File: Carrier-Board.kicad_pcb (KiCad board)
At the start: 4 copper layers, 92 x 96 mm, 50 parts, among them J1 CONN_3-6318491-6, J10 Conn_02x03_Odd_Even, J2 Conn_01x0, J3 Conn_02x26_Odd_Even, J4 SI-51009-F, J5 Conn_02x26_Odd_Even, J6 Conn_01x03_Male, J7 Conn_01x03_Male, J8 Conn_01x06_Male, J9 Conn_02x04_Odd_Even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

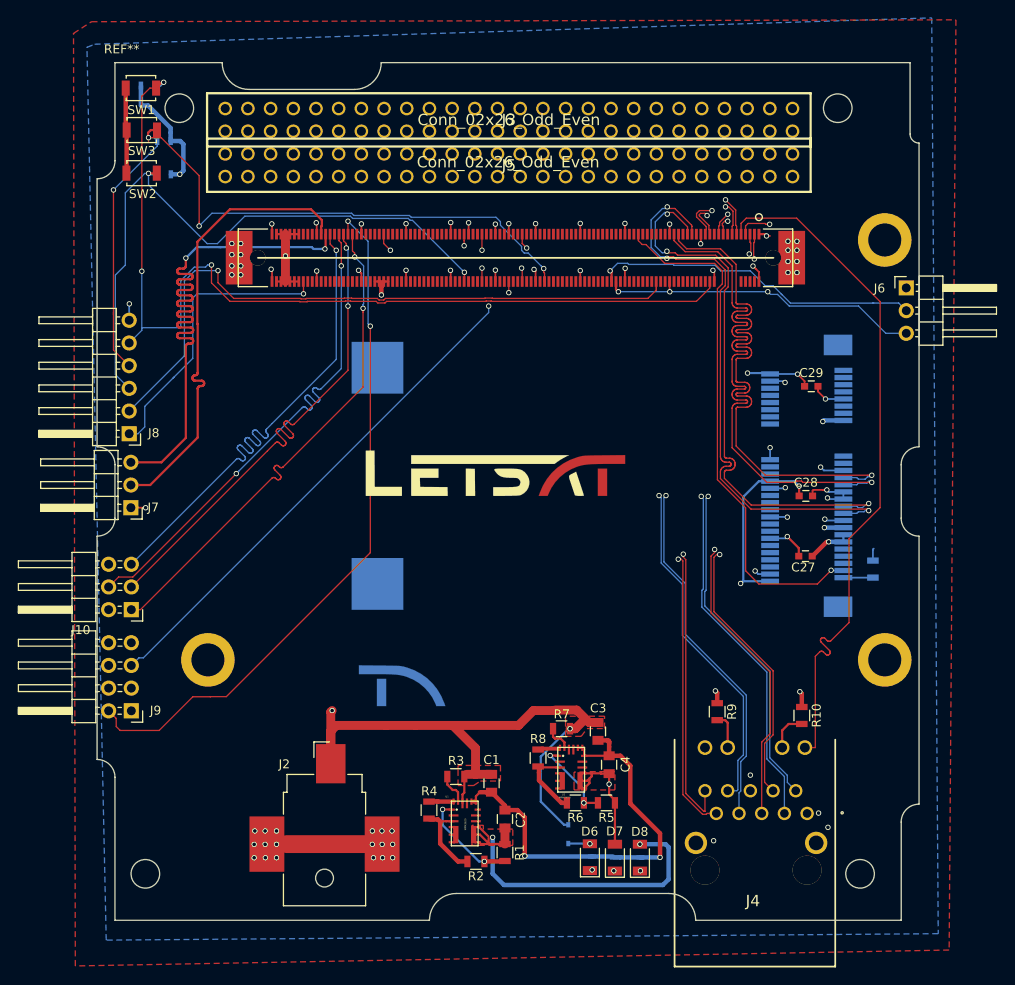
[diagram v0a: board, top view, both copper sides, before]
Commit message: Fix DRC and unconnected tracks
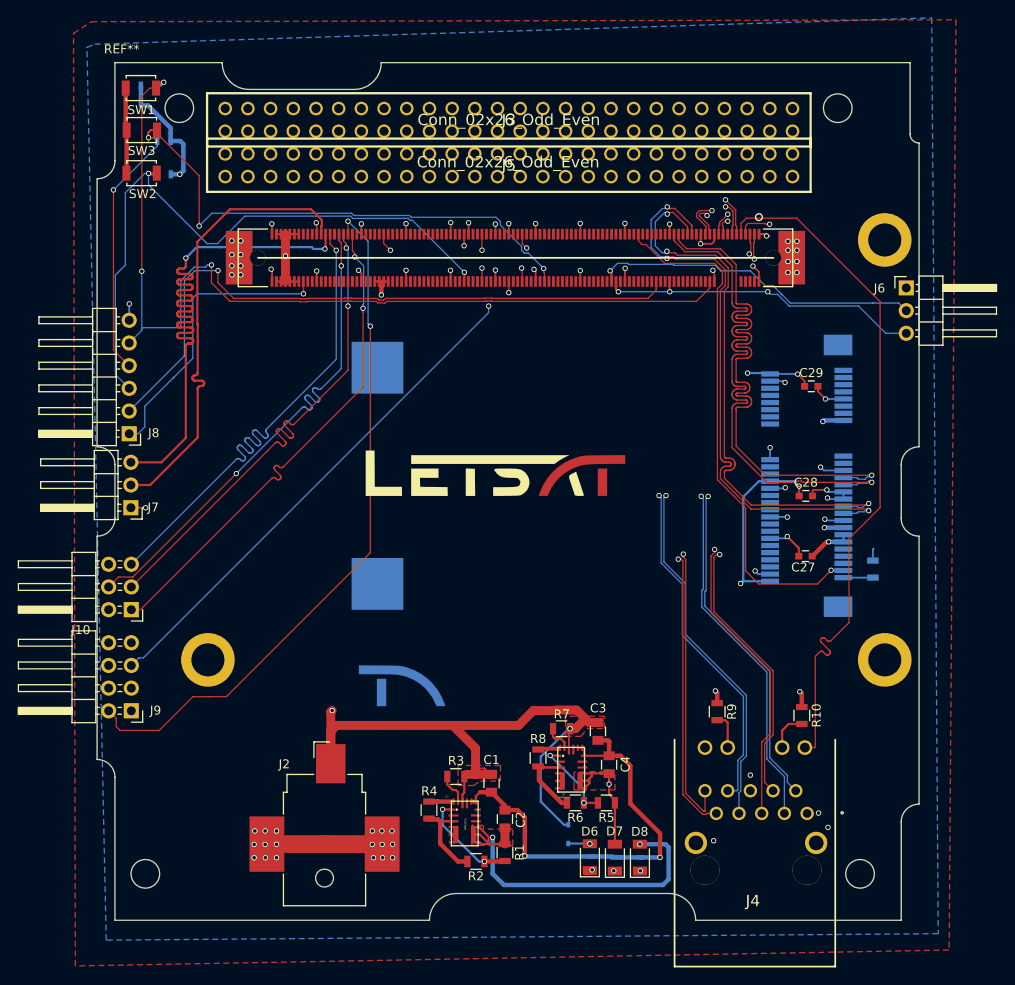
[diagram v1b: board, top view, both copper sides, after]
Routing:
- net GBE0_CTREF(GND): track 166.6 -> 187.5 mm
- net mCOM_12V: track 143.3 -> 147.8 mm
- net GNDA: track 17.2 -> 19.7 mm
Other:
- rule pad_to_mask_clearance: 0.2 -> 0.05
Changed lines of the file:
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@@
   (general
     (links 180)
-    (no_connects 5)
+    (no_connects 3)
     (area 71.442618 18.99 188.200001 129.325001)
     (thickness 1.6)
     (drawings 7)
-    (tracks 3697)
+    (tracks 3713)
     (zones 0)
     (modules 50)
@@
   (layers
     (0 F.Cu signal)
-    (1 In1.Cu power)
-    (2 In2.Cu power)
+    (1 In1.Cu power hide)
+    (2 In2.Cu power hide)
     (31 B.Cu signal)
     (32 B.Adhes user)
@@
     (pad_size 6 6)
     (pad_drill 3.7)
-    (pad_to_mask_clearance 0.2)
+    (pad_to_mask_clearance 0.05)
     (aux_axis_origin 0 0)
     (grid_origin 128.775 45.85)
@@
   (segment (start 125.27 113.415) (end 127.52 113.415) (width 0.5) (layer F.Cu) (net 9))
   (segment (start 127.52 113.415) (end 127.57 113.365) (width 0.25) (layer F.Cu) (net 9))
+  (segment (start 133.73 102.896392) (end 131.391392 102.896392) (width 0.2) (layer F.Cu) (net 10))
+  (segment (start 131.391392 102.896392) (end 131.28 102.785) (width 0.2) (layer F.Cu) (net 10))
   (segment (start 134.505 106.86) (end 133.905 106.86) (width 0.5) (layer F.Cu) (net 10))
   (segment (start 133.905 106.86) (end 131.38 104.335) (width 0.5) (layer F.Cu) (net 10))
@@
   (segment (start 121.12 104.815) (end 121.72 105.415) (width 0.25) (layer F.Cu) (net 11))
   (segment (start 119.145 106.69) (end 120.045 106.69) (width 0.5) (layer F.Cu) (net 12))
-  (segment (start 119.97 106.715) (end 121.82 106.715) (width 0.5) (layer F.Cu) (net 12))
+  (segment (start 119.885 106.715) (end 121.735 106.715) (width 0.5) (layer F.Cu) (net 12))
   (segment (start 137.98 106.86) (end 136.405 106.86) (width 0.25) (layer F.Cu) (net 13))
   (segment (start 132.63 101.56) (end 133.493608 101.56) (width 0.25) (layer F.Cu) (net 13))
@@
   (segment (start 153.334058 68.989003) (end 153.334058 68.910996) (width 0.127) (layer F.Cu) (net 19))
   (segment (start 145.875001 45.285001) (end 145.7 45.11) (width 0.25) (layer F.Cu) (net 19))
-  (segment (start 168.29 73.35) (end 168.114999 73.525001) (width 0.25) (layer F.Cu) (net 19))
+  (segment (start 168.29 73.35) (end 168.114999 73.525001) (width 0.127) (layer F.Cu) (net 19))
   (segment (start 145.443199 40.774999) (end 144.398198 41.82) (width 0.127) (layer B.Cu) (net 19))
   (segment (start 144.398198 41.82) (end 144.398198 44.515) (width 0.127) (layer B.Cu) (net 19))
@@
   (segment (start 167.125 73.825) (end 167.576802 73.825) (width 0.127) (layer B.Cu) (net 19))
   (segment (start 167.576802 73.825) (end 167.876801 73.525001) (width 0.127) (layer B.Cu) (net 19))
-  (segment (start 168.114999 73.525001) (end 168.29 73.35) (width 0.25) (layer B.Cu) (net 19))
+  (segment (start 168.114999 73.525001) (end 168.29 73.35) (width 0.127) (layer B.Cu) (net 19))
   (segment (start 146.436801 45.734999) (end 145.875001 45.734999) (width 0.127) (layer F.Cu) (net 20))
   (segment (start 151.027463 46.005) (end 146.706802 46.005) (width 0.127) (layer F.Cu) (net 20))
@@
   (segment (start 167.763198 74.275) (end 168.063199 73.974999) (width 0.127) (layer B.Cu) (net 20))
   (segment (start 167.125 74.275) (end 167.763198 74.275) (width 0.127) (layer B.Cu) (net 20))
-  (segment (start 168.063199 73.974999) (end 168.114999 73.974999) (width 0.25) (layer B.Cu) (net 20))
+  (segment (start 168.140899 73.974999) (end 168.192699 73.974999) (width 0.25) (layer B.Cu) (net 20))
   (segment (start 154.51 73.84) (end 151.35 70.68) (width 0.127) (layer F.Cu) (net 21))
   (segment (start 162.54 82.36) (end 155.99 82.36) (width 0.127) (layer F.Cu) (net 21))
@@
   (via (at 105.02 49.88) (size 0.6) (drill 0.4) (layers F.Cu B.Cu) (net 36))
   (segment (start 92.63 57.1) (end 92.63 50.35) (width 0.127) (layer B.Cu) (net 36))
+  (segment (start 134.73 100.896392) (end 134.73 98.685) (width 0.2) (layer F.Cu) (net 37))
+  (segment (start 134.73 98.685) (end 134.855 98.56) (width 0.2) (layer F.Cu) (net 37))
+  (segment (start 124.28 100.74) (end 124.28 103) (width 1) (layer F.Cu) (net 37))
+  (segment (start 124.28 103) (end 124.28 103.665) (width 1) (layer F.Cu) (net 37))
+  (segment (start 126.07 103.665) (end 125.945 103.665) (width 0.2) (layer F.Cu) (net 37))
+  (segment (start 125.945 103.665) (end 125.28 103) (width 0.2) (layer F.Cu) (net 37))
+  (segment (start 125.28 103) (end 124.28 103) (width 0.2) (layer F.Cu) (net 37))
   (segment (start 108.71 98.19) (end 108.075 98.825) (width 1) (layer F.Cu) (net 37))
   (segment (start 135.6 96.47) (end 136.99 97.86) (width 1) (layer F.Cu) (net 37))
@@
   (segment (start 124.28 103.665) (end 123.27 103.665) (width 0.25) (layer F.Cu) (net 37))
   (segment (start 121.73 98.19) (end 124.28 100.74) (width 1) (layer F.Cu) (net 37))
-  (segment (start 124.28 100.74) (end 124.28 103.665) (width 1) (layer F.Cu) (net 37))
   (segment (start 117.595 98.19) (end 121.73 98.19) (width 1) (layer F.Cu) (net 37))
   (segment (start 114.26 98.19) (end 117.595 98.19) (width 1) (layer F.Cu) (net 37))
@@
   (segment (start 122.82 105.915) (end 122.82 106.915) (width 0.25) (layer F.Cu) (net 37))
   (segment (start 123.02 103.915) (end 123.02 105.715) (width 0.25) (layer F.Cu) (net 37))
+  (segment (start 103.125 111.475) (end 107.185 111.475) (width 2) (layer F.Cu) (net 38))
+  (segment (start 107.185 111.475) (end 113.825 111.475) (width 2) (layer F.Cu) (net 38))
+  (segment (start 113.825 111.5) (end 107.21 111.5) (width 0.2) (layer F.Cu) (net 38))
+  (segment (start 107.21 111.5) (end 107.185 111.475) (width 0.2) (layer F.Cu) (net 38))
+  (segment (start 113.825 111.5) (end 102 111.5) (width 0.2) (layer F.Cu) (net 38))
+  (segment (start 150.999999 43.2) (end 150.999999 43.9969) (width 0.2) (layer F.Cu) (net 38))
+  (segment (start 150.999999 43.9969) (end 150.721899 44.275) (width 0.2) (layer F.Cu) (net 38))
+  (segment (start 150.721899 44.275) (end 149.899264 44.275) (width 0.2) (layer F.Cu) (net 38))
+  (segment (start 149.899264 44.275) (end 149.475 44.275) (width 0.2) (layer F.Cu) (net 38))
   (segment (start 159.665996 44.333) (end 159.665996 45.833) (width 0.25) (layer F.Cu) (net 38))
   (segment (start 159.665996 45.833) (end 158.447695 47.051301) (width 0.25) (layer F.Cu) (net 38))
@@
   (via (at 160.25 45) (size 0.6) (drill 0.4) (layers F.Cu B.Cu) (net 38))
   (via (at 160.25 44) (size 0.6) (drill 0.4) (layers F.Cu B.Cu) (net 38))
-  (via (at 98 44.25) (size 0.6) (drill 0.4) (layers F.Cu B.Cu) (net 38))
+  (via (at 98 43.945) (size 0.6) (drill 0.4) (layers F.Cu B.Cu) (net 38))
   (via (at 98 45.5) (size 0.6) (drill 0.4) (layers F.Cu B.Cu) (net 38))
   (via (at 98 46.75) (size 0.6) (drill 0.4) (layers F.Cu B.Cu) (net 38))
@@
   (via (at 97 46.75) (size 0.6) (drill 0.4) (layers F.Cu B.Cu) (net 38))
   (via (at 97 45.5) (size 0.6) (drill 0.4) (layers F.Cu B.Cu) (net 38))
-  (via (at 97 44.25) (size 0.6) (drill 0.4) (layers F.Cu B.Cu) (net 38))
+  (via (at 97 43.945) (size 0.6) (drill 0.4) (layers F.Cu B.Cu) (net 38))
   (segment (start 156.85 43.4) (end 157.232996 43.4) (width 0.2) (layer F.Cu) (net 38))
   (segment (start 159.240986 45.40799) (end 159.240986 45.656956) (width 0.2) (layer F.Cu) (net 38))
@@
   (segment (start 155.04 105.5) (end 154.845001 105.694999) (width 0.25) (layer B.Cu) (net 38))
   (segment (start 100.925 111.475) (end 103.125 111.475) (width 0.5) (layer F.Cu) (net 38))
-  (segment (start 103.125 111.475) (end 113.825 111.475) (width 2) (layer F.Cu) (net 38))
   (segment (start 137.255 112.935) (end 137.33 112.86) (width 0.25) (layer B.Cu) (net 38))
   (segment (start 85.225 31.55) (end 85.225 36.35) (width 0.5) (layer F.Cu) (net 38))

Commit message: asdasdasdasd
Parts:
- J3, J5: value Conn_02x26_Odd_Even -> (none)
- U9: value MSATA-Socket -> (none)
- renumbered REF** to ?

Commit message: no shorts i think
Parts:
- moved J9 2.03 mm to (87.8, 96.7)
- moved J10 1.83 mm to (87.6, 85.2)
- moved J7 1.64 mm to (87.3, 73.8)
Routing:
- net GPO0: track 78.6 -> 74.2 mm
- net GBE0_CTREF(GND): track 187.6 -> 190.3 mm, vias 83 -> 84
- net mCOM_RX: track 51.0 -> 48.9 mm
- net GPO1: track 80.5 -> 78.5 mm
- net +3.3V: track 203.6 -> 201.8 mm
- net GPI0: track 84.5 -> 82.7 mm
- net mCOM_TX: track 66.4 -> 64.6 mm
- net GPO3: track 75.1 -> 73.9 mm
- net GPI2: track 66.8 -> 65.9 mm
- net GPO2: track 75.2 -> 74.4 mm
- net SPI_MISO: track 56.0 -> 55.2 mm
- net SPI_CLK: track 56.0 -> 55.2 mm
- net SPI_CS#: track 56.0 -> 55.2 mm
- net GPI3: track 75.0 -> 74.3 mm
